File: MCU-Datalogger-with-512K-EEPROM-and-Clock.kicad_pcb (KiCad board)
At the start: 2 copper layers, 25 parts, among them J1 Conn_01x04_Pin, J2 Conn_01x04_Pin, J3 Conn_01x09_Pin, J4 Conn_02x03_Odd_Even, U1 24LC1025, U2 24LC1025, U3 ATMEGA328P-AU, U4 DS1337S_, Y1 32.768 KHz, Y2 16 MHz

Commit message: remove the current board
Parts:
- removed BT1: Battery, Connector_PinHeader_2.54mm:PinHeader_1x02_P2.54mm_Vertical
- removed C1, C4: 0.1uF, Capacitor_SMD:C_0805_2012Metric
- removed C2, C3: 22pF, Capacitor_SMD:C_0805_2012Metric
- removed C5: 100nF, Capacitor_SMD:C_0805_2012Metric
- removed D1, D2: LED, LED_SMD:LED_0805_2012Metric
- removed J1, J2: Conn_01x04_Pin, Connector_PinHeader_2.54mm:PinHeader_1x04_P2.54mm_Vertical
- removed J3: Conn_01x09_Pin, Connector_PinHeader_2.54mm:PinHeader_1x09_P2.54mm_Vertical
- removed J4: Conn_02x03_Odd_Even, Connector_PinHeader_2.54mm:PinHeader_2x03_P2.54mm_Vertical
- removed R1, R2, R6: 10K, Resistor_SMD:R_0805_2012Metric
- removed R3, R4: 4.7K, Resistor_SMD:R_0805_2012Metric
- removed R5, R7: 330, Resistor_SMD:R_0805_2012Metric
- removed U1, U2: 24LC1025, Package_SO:SOIC-8_5.3x5.3mm_P1.27mm
- removed U3: ATMEGA328P-AU, ATMEGA328P-AU:QFP80P900X900X120-32N
- removed U4: DS1337S_, DS1337S_:SOIC127P600X175-8N
- removed Y1: 32.768 KHz, Crystal:Crystal_SMD_5032-2Pin_5.0x3.2mm_HandSoldering
- removed Y2: 16 MHz, Crystal:Crystal_SMD_5032-2Pin_5.0x3.2mm_HandSoldering
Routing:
- net /Vcc: track 91.8 -> 0.00 mm
- net GND: track 72.4 -> 0.00 mm, vias 2 -> 0
- net /SCL: track 64.5 -> 0.00 mm
- net Net-(BT1-+): track 60.1 -> 0.00 mm, vias 3 -> 0
- net /SDA: track 35.1 -> 0.00 mm
- net /D2: track 29.7 -> 0.00 mm, vias 1 -> 0
- net /D3: track 26.5 -> 0.00 mm, vias 2 -> 0
- net /TX: track 26.0 -> 0.00 mm, vias 1 -> 0
- net Net-(U3-PB7): track 24.4 -> 0.00 mm, vias 2 -> 0
- net /D4: track 23.7 -> 0.00 mm, vias 3 -> 0
- net /RX: track 23.5 -> 0.00 mm, vias 1 -> 0
- net /MOSI: track 23.5 -> 0.00 mm, vias 1 -> 0
- net Net-(U3-PB6): track 20.4 -> 0.00 mm
- net /RESET: track 20.4 -> 0.00 mm, vias 2 -> 0
- net /MISO: track 19.4 -> 0.00 mm, vias 1 -> 0
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- removed copper zone on F.Cu, net /Vcc
- removed copper zone on B.Cu, net GND

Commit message: components added; now creating the branches
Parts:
- added BT1: Battery, Connector_PinHeader_2.54mm:PinHeader_1x02_P2.54mm_Vertical, F.Cu at (140.8, 95.6)
- added C1: 0.1uF, Capacitor_SMD:C_0805_2012Metric, F.Cu at (136.3, 88.3)
- added C2: 22pF, Capacitor_SMD:C_0805_2012Metric, F.Cu at (136.3, 91.3)
- added C3: 22pF, Capacitor_SMD:C_0805_2012Metric, F.Cu at (136.3, 94.3)
- added C4: 0.1uF, Capacitor_SMD:C_0805_2012Metric, F.Cu at (136.3, 97.3)
- added C5: 100nF, Capacitor_SMD:C_0805_2012Metric, F.Cu at (136.3, 100.3)
- added D1: LED, LED_SMD:LED_0805_2012Metric, F.Cu at (145.4, 94.8)
- added D2: LED, LED_SMD:LED_0805_2012Metric, F.Cu at (145.4, 97.9)
- added J1: Conn_01x04_Pin, Connector_PinHeader_2.54mm:PinHeader_1x04_P2.54mm_Vertical, F.Cu at (156.8, 75.4)
- added J2: Conn_01x04_Pin, Connector_PinHeader_2.54mm:PinHeader_1x04_P2.54mm_Vertical, F.Cu at (161.5, 75.4)
- added J3: Conn_01x09_Pin, Connector_PinHeader_2.54mm:PinHeader_1x09_P2.54mm_Vertical, F.Cu at (152.2, 75.4)
- added J4: Conn_02x03_Odd_Even, Connector_PinHeader_2.54mm:PinHeader_2x03_P2.54mm_Vertical, F.Cu at (156.8, 87.6)
- added R1: 10K, Resistor_SMD:R_0805_2012Metric, F.Cu at (121.6, 74.5)
- added R2: 10K, Resistor_SMD:R_0805_2012Metric, F.Cu at (121.6, 77.5)
- added R3: 4.7K, Resistor_SMD:R_0805_2012Metric, F.Cu at (121.6, 80.4)
- added R4: 4.7K, Resistor_SMD:R_0805_2012Metric, F.Cu at (121.6, 83.4)
- added R5: 330, Resistor_SMD:R_0805_2012Metric, F.Cu at (121.6, 86.3)
- added R6: 10K, Resistor_SMD:R_0805_2012Metric, F.Cu at (121.6, 89.3)
- added R7: 330, Resistor_SMD:R_0805_2012Metric, F.Cu at (121.6, 92.2)
- added U1: 24LC1025, Package_SO:SOIC-8_5.3x5.3mm_P1.27mm, F.Cu at (129.0, 76.5)
- added U2: 24LC1025, Package_SO:SOIC-8_5.3x5.3mm_P1.27mm, F.Cu at (129.0, 83.3)
- added U3: ATMEGA328P-AU, ATMEGA328P-AU:QFP80P900X900X120-32N, F.Cu at (140.7, 78.7)
- added U4: DS1337S_, DS1337S_:SOIC127P600X175-8N, F.Cu at (143.6, 90.0)
- added Y1: 32.768 KHz, Crystal:Crystal_SMD_5032-2Pin_5.0x3.2mm_HandSoldering, F.Cu at (128.9, 89.2)
- added Y2: 16 MHz, Crystal:Crystal_SMD_5032-2Pin_5.0x3.2mm_HandSoldering, F.Cu at (128.9, 94.0)

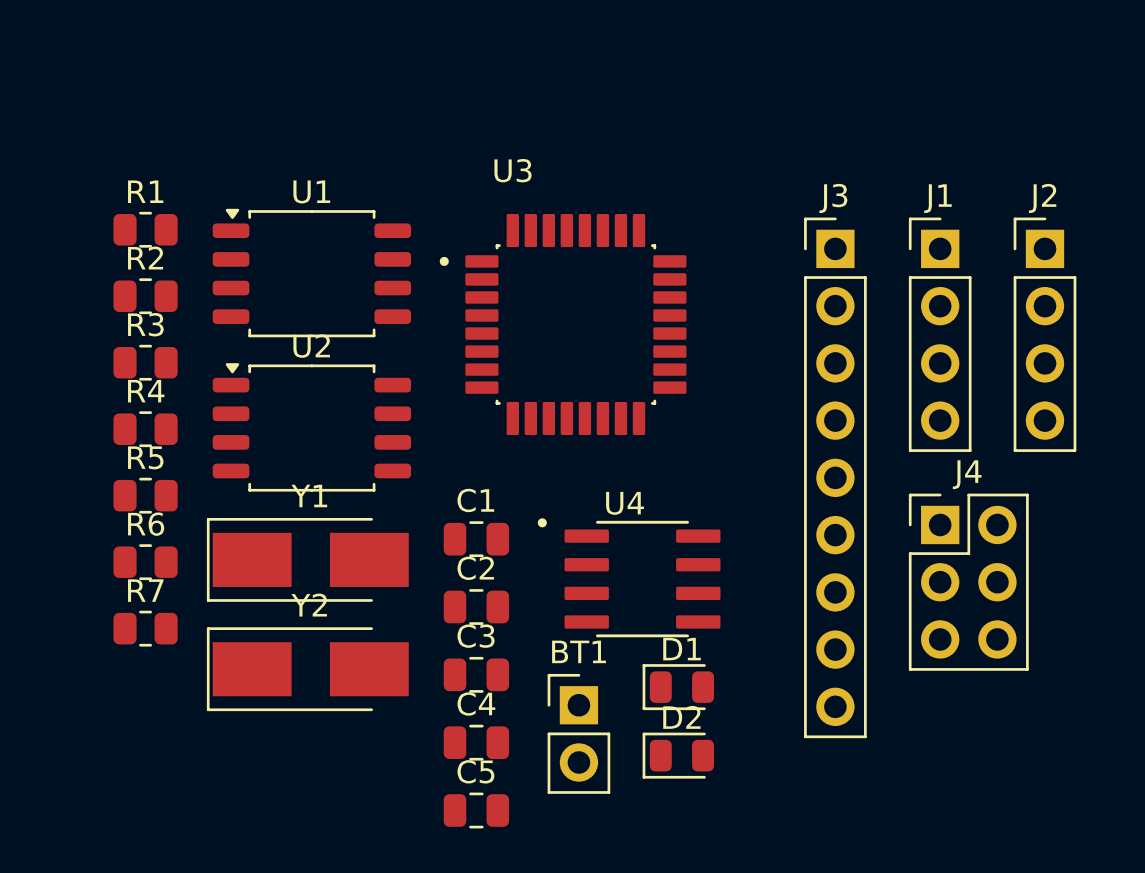
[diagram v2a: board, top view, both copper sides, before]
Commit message: pcb components layed out; requires routing
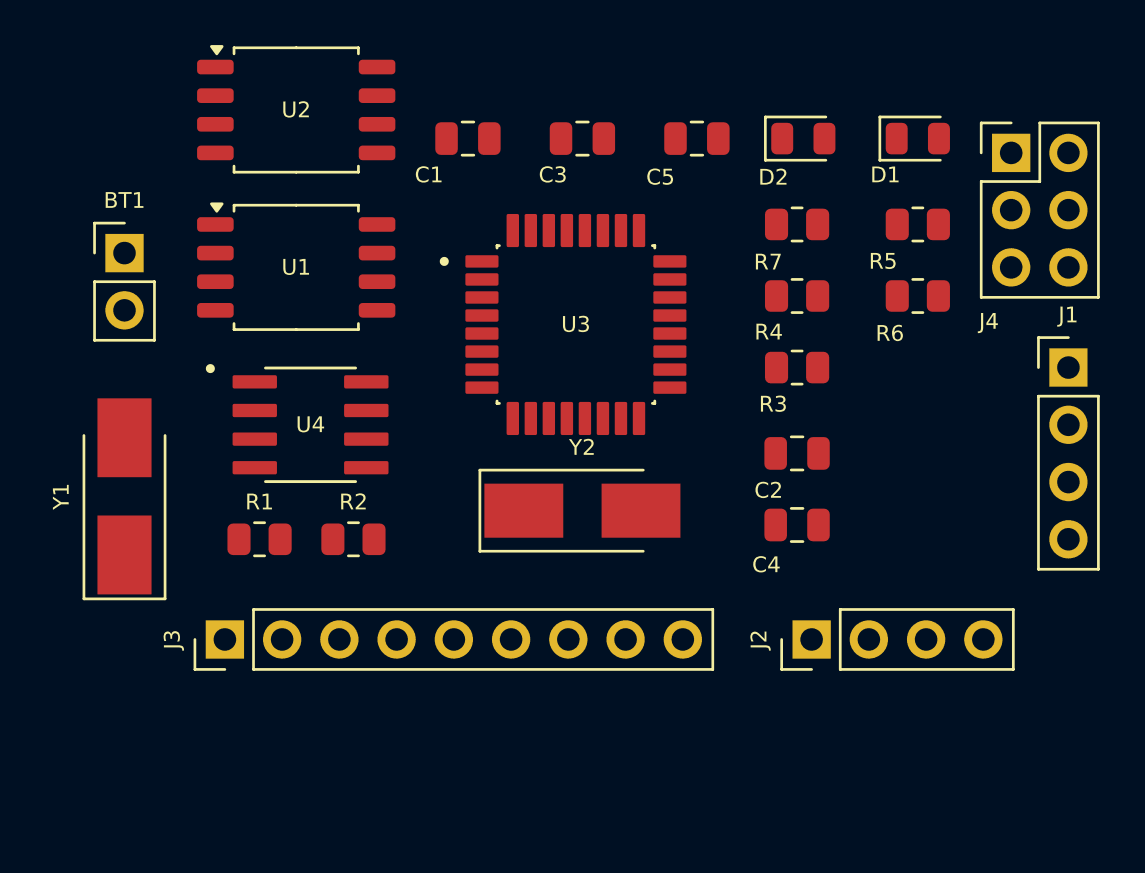
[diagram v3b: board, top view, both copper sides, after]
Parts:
- moved R5 36.3 mm to (155.9, 74.3)
- moved R6 36.2 mm to (155.9, 77.5)
- moved R7 34.0 mm to (150.5, 74.3)
- moved J3 32.2 mm to (125.1, 92.7), turned to 90 degrees
- moved C5 31.4 mm to (146.1, 70.5)
- moved R4 29.5 mm to (150.5, 77.5)
- moved R3 28.9 mm to (150.5, 80.6)
- moved BT1 28.4 mm to (120.7, 75.6)
- moved D2 27.9 mm to (150.8, 70.5)
- moved D1 26.5 mm to (155.9, 70.5)
- moved C3 24.3 mm to (141.0, 70.5)
- moved J2 20.2 mm to (151.1, 92.7), turned to 90 degrees
- moved C1 17.8 mm to (135.9, 70.5)
- moved C4 17.2 mm to (150.5, 87.6)
- moved J4 16.8 mm to (160.0, 71.1)
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
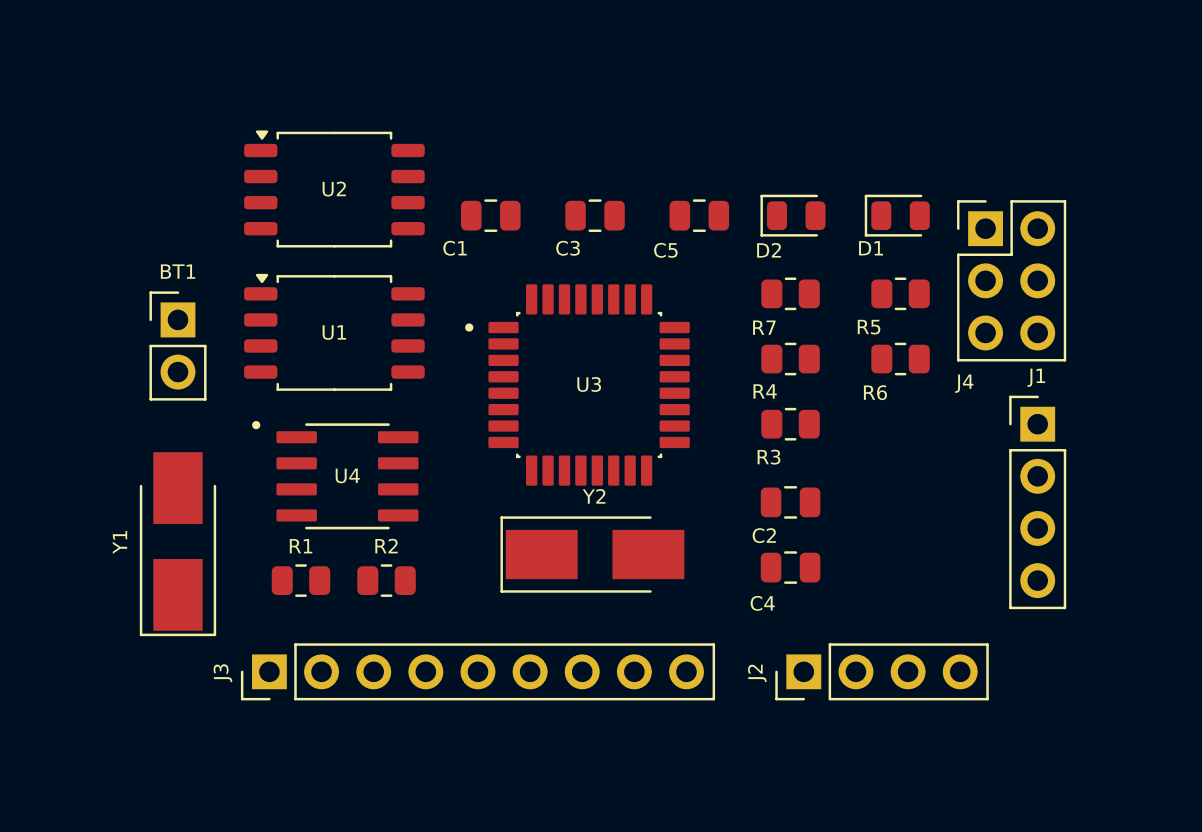
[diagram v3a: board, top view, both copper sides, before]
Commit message: 2 layer board completed; minus annotation and further design rule checking
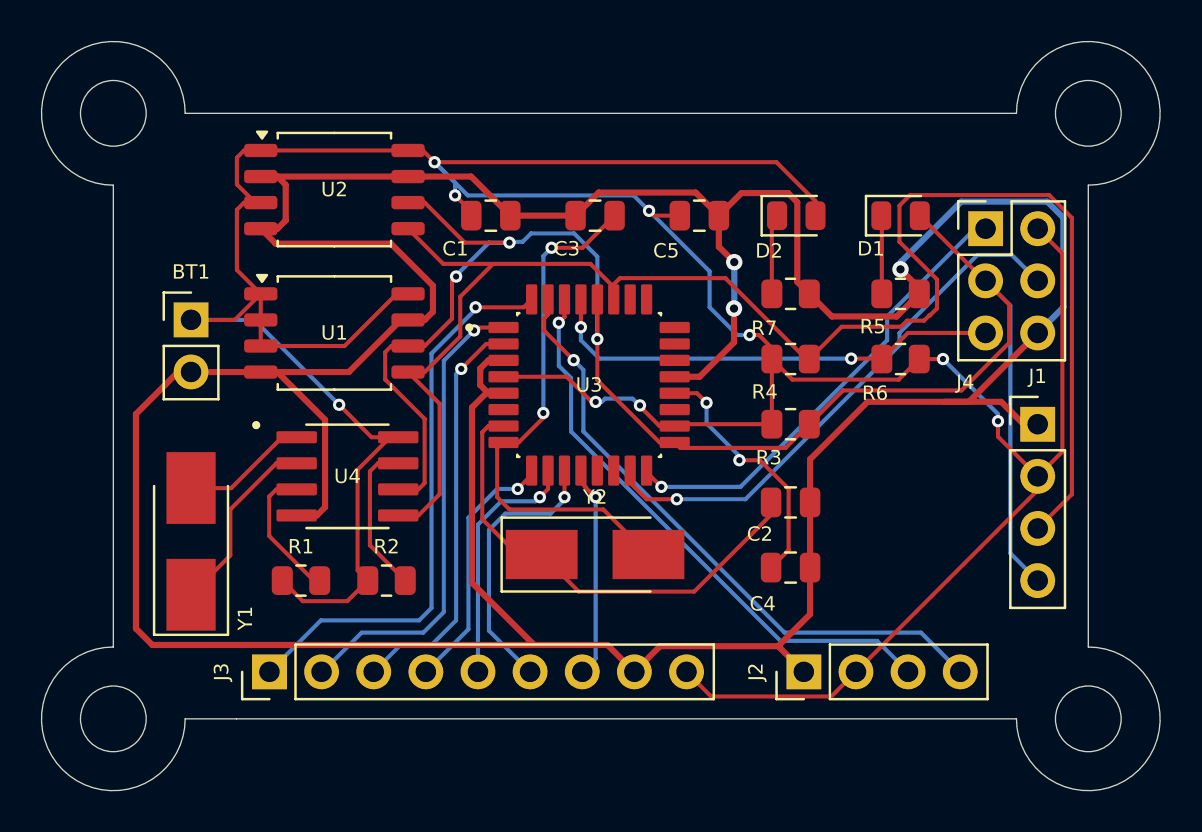
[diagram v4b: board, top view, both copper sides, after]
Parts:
- added REF**: MountingHole_3.2mm_M3, MountingHole:MountingHole_3.2mm_M3, F.Cu at (165.0, 65.5)
- added REF**: MountingHole_3.2mm_M3, MountingHole:MountingHole_3.2mm_M3, F.Cu at (117.5, 65.5)
- added REF**: MountingHole_3.2mm_M3, MountingHole:MountingHole_3.2mm_M3, F.Cu at (117.5, 95.0)
- added REF**: MountingHole_3.2mm_M3, MountingHole:MountingHole_3.2mm_M3, F.Cu at (165.0, 95.0)
- moved BT1 0.64 mm to (121.3, 75.6)
- moved Y1 0.64 mm to (121.3, 86.4)
- turned C2 to 180 degrees
- turned C3 to 180 degrees
- turned R5 to 180 degrees
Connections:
- BT1 pad 1: Net-(BT1-+) -> /Vcc
- C5 pad 1: Net-(BT1-+) -> /Vcc
- D2 pad 2: Net-(BT1-+) -> /Vcc
- U3 pad 18: Net-(BT1-+) -> /Vcc
- U3 pad 4: Net-(BT1-+) -> /Vcc
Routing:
- net GND: track 0.00 -> 200.2 mm, vias 0 -> 3
- net /Vcc: track 0.00 -> 176.9 mm, vias 0 -> 9
- net /SCL: track 0.00 -> 83.8 mm, vias 0 -> 3
- net /SDA: track 0.00 -> 78.2 mm
- net /TX: track 0.00 -> 30.5 mm, vias 0 -> 1
- net /RX: track 0.00 -> 28.1 mm, vias 0 -> 1
- net /D2: track 0.00 -> 27.6 mm, vias 0 -> 1
- net /MOSI: track 0.00 -> 26.6 mm, vias 0 -> 1
- net Net-(U3-PB7): track 0.00 -> 26.0 mm, vias 0 -> 2
- net /MISO: track 0.00 -> 23.6 mm, vias 0 -> 1
- net Net-(U3-PB6): track 0.00 -> 23.1 mm
- net /D3: track 0.00 -> 23.0 mm, vias 0 -> 1
- net /RESET: track 0.00 -> 22.6 mm, vias 0 -> 2
- net /D4: track 0.00 -> 20.0 mm, vias 0 -> 1
- net /D7: track 0.00 -> 13.4 mm, vias 0 -> 1
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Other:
- board outline added: 54.5 x 36.5 mm

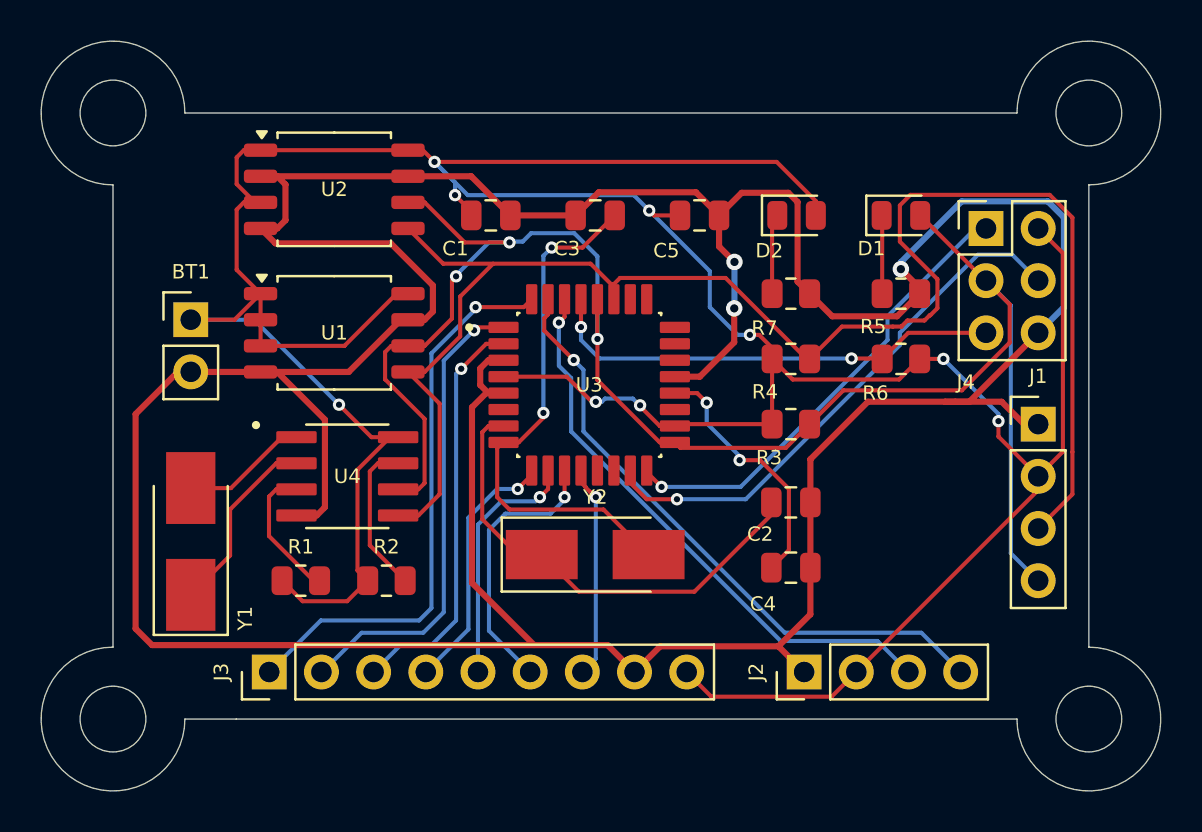
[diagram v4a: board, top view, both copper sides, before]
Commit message: 2layer board completed with DRC completed[only small text constraint left]
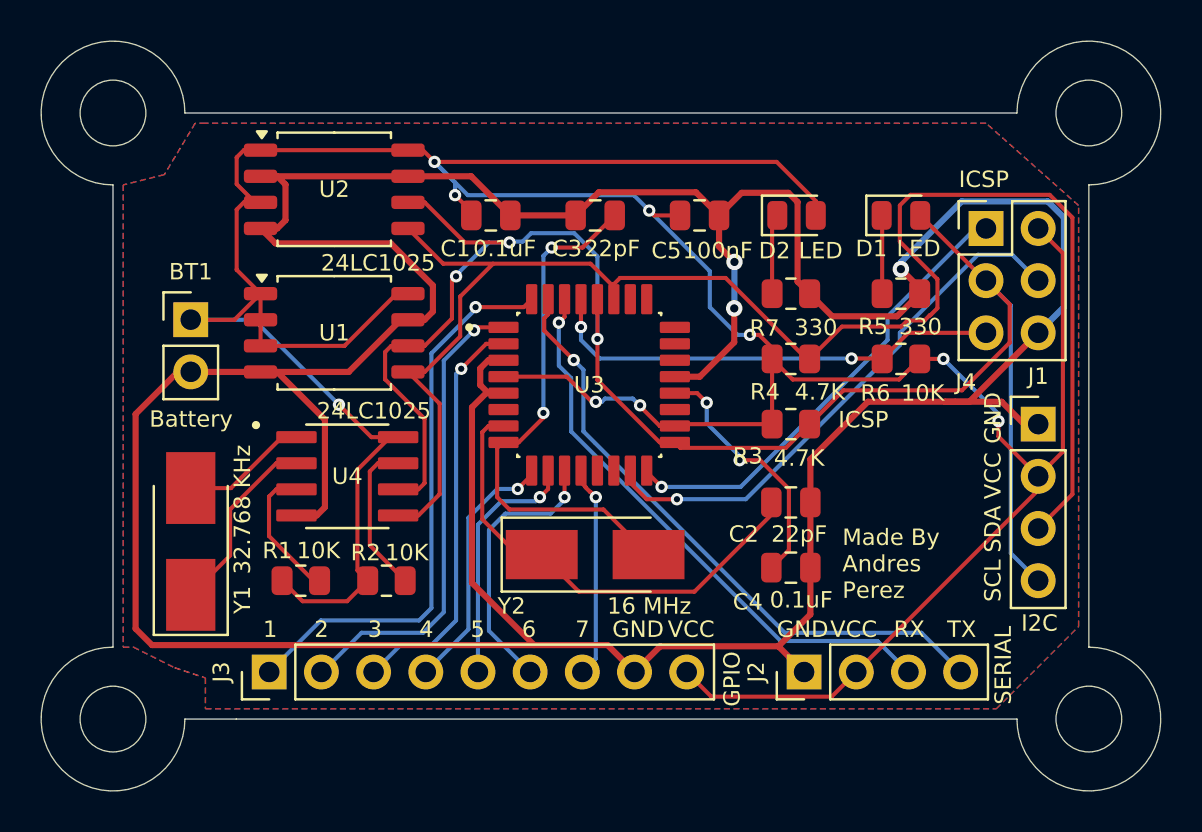
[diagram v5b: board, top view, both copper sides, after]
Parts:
- added REF**: KiCad-Logo2_6mm_SilkScreen, Symbol:KiCad-Logo2_6mm_SilkScreen, B.Cu at (127.0, 85.5)
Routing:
- added copper zone on F.Cu, net /Vcc
- added copper zone on B.Cu, net GND
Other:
- board text added: "1"
- board text added: "2"
- board text added: "3"
- board text added: "4"
- board text added: "5"
- board text added: "6"
- board text added: "7"
- board text added: "GND"
- board text added: "GPIO"
- board text added: "I2C"
- board text added: "ICSP"
- board text added: "Made By Andres Perez"
- board text added: "RX"
- board text added: "SCL"
- board text added: "SDA"
- board text added: "SERIAL"
- board text added: "TX"
- board text added: "VCC"

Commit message: 4layer board completed
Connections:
- D1 pad 2: /SCL -> /SCK
- J4 pad 3: /SCL -> /SCK
- U3 pad 17: /SCL -> /SCK
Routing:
- net GND: track 200.2 -> 38.3 mm, vias 3 -> 11
- net /Vcc: track 176.9 -> 38.2 mm, vias 9 -> 13
- net /SCK: track 0.00 -> 24.6 mm, vias 0 -> 1
- net /SCL: track 83.8 -> 59.8 mm
- net /SDA: track 78.2 -> 58.0 mm, vias 0 -> 3
- net /D8: track 10.4 -> 17.7 mm, vias 1 -> 0
- net /TX: track 30.5 -> 37.0 mm, vias 1 -> 0
- net /RX: track 28.1 -> 33.5 mm, vias 1 -> 0
- net Net-(U3-PB6): track 23.1 -> 19.8 mm, vias 0 -> 3
- net /MOSI: track 26.6 -> 27.9 mm
- net Net-(U3-AREF): track 12.4 -> 11.4 mm
- net Net-(U4-~{INTA}): track 6.76 -> 5.86 mm
- net Net-(U3-PB7): track 26.0 -> 26.8 mm, vias 2 -> 3
- net /D3: track 23.0 -> 22.8 mm, vias 1 -> 0
- net /D5: track 12.5 -> 12.7 mm, vias 1 -> 0
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- added copper zone on In2.Cu, net /Vcc
- removed copper zone on F.Cu, net /Vcc
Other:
- copper layers 2 -> 4
